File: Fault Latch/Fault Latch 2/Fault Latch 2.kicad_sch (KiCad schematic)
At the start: 47 parts, among them J1 Inputs, K1 Fujitsu_FTR-LYAA005x, K2 Fujitsu_FTR-LYAA005x, K3 Fujitsu_FTR-LYAA005x, Q1 PMOS, Q2 PMOS, Q3 PMOS, Q4 NMOS, Q5 PMOS, Q6 PMOS, Q7 PMOS, Q8 NMOS, Q9 PMOS, SW1 SW_Push_Dual_x2, SW2 SW_Push_Dual_x2, SW4 SW_Push_Dual_x2, U1 74LS279, U10 74LS279, U11 4N35, U2 74AHC1G04, U3 74AHC1G04, U5 74LS279, U7 4N35, U8 4N35, U9 74AHC1G04

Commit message: Edits to Fault Latch and TSSI
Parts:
- removed D3: LED, symbol Device:LED
- removed Q1, Q2, Q3, Q6: PMOS, symbol Simulation_SPICE:PMOS
- removed R1: 2.2k, symbol Device:R_US
- removed R2, R4: R_US, symbol Device:R_US
- removed SW2, SW4: SW_Push_Dual_x2, symbol Switch:SW_Push_Dual_x2
- removed U1, U10, U5: 74LS279, symbol 74xx:74LS279
- removed U11, U7, U8: 4N35, Package_DIP:DIP-6_W7.62mm, symbol Isolator:4N35
- removed U3: 74AHC1G04, symbol 74xGxx:74AHC1G04
- added C101: 100n, symbol Device:C
- added C102: ?, symbol Device:C
- added D101: LED, symbol Device:LED
- added Q101, Q104, Q108: NMOS, symbol Simulation_SPICE:NMOS
- added R101, R102, R107, R108: 10k, symbol Device:R_US
- added R103: 500R, symbol Device:R_US
- added R106: 2.2k, symbol Device:R_US
- added R109: ?, symbol Device:R_US
- added R114: R_US, symbol Device:R_US
- added U103: 74AHC1G00, symbol 74xGxx:74AHC1G00
- added U104: 74LS279, symbol 74xx:74LS279
- added U105: SFH617A-1, Package_DIP:DIP-4_W7.62mm, symbol Isolator:SFH617A-1
- renumbered D1 to D102, D4 to D103, D5 to D104, D6 to D105, D2 to D106, J1 to J101, J4 to J102, J3 to J103, J2 to J104, K3 to K101, K2 to K102, K1 to K103, Q8 to Q102, Q4 to Q103, Q7 to Q105, Q9 to Q106, Q5 to Q107, R3 to R104, R8 to R105, R6 to R110, R9 to R111, R7 to R112, R5 to R113, R10 to R115, R13 to R116, R12 to R117, R11 to R118, SW1 to SW101, U2 to U101, U9 to U102
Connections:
- net +5V: now also R103.1, R107.1, R108.2, R114.2, U103.5 (VCC), U104.16 (VCC); no longer D106.1 (K), K103.A1
- net BSPD: now also R102.1
- net GND: now also SW101.1 (C), C102.2, Q101.3 (S), Q104.3 (S), Q108.3 (S), R102.2, R106.2, U103.3 (GND), U104.8 (GND), U105.3; no longer R115.1
- net IMD: now also R106.1
- net Shutdown Circuit: no longer J104.1 (Pin_1), K103.13
- net at D106.2 (A), K103.A2: now also Q108.1 (D)
- net +12V: now reaches R115.2
- net +12V: now also D106.1 (K), K103.A1, R101.1
- net at SW101.2 (D): now also R108.1, R109.2
- net at D104.2 (A), K102.A2: no longer Q107.1 (D)
- net BMS renamed NBMS
- net NBMS: now also R101.2
- new net: C101.2, D101.1 (K), Q101.1 (D), Q104.2 (G)
- new net: J104.1 (Pin_1), K103.13
- new net: Q108.2 (G), R115.1, U105.4
- new net: C101.1, D101.2 (A), R103.2
- new net: U103.4, U104.2 (~{S}), U104.3 (~{S})
- new net: R114.1, U105.1
- new net: U104.4 (Q), U105.2
- new net NBMS_HV: Q101.2 (G)
- new net NBMS_LV: Q104.1 (D), R107.2, U103.1, U104.1 (~{R})
- new net NRESET: C102.1, R109.1, U103.2
- no-connect marks 4 -> 3
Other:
- note added: "16mA MAX"
- note added: "I think FSAE says relays need to be normally activated?"
- note added: "Open collector pull ups/downs should be provided on this board only!"
- note added: "When nR pulsed low (fault), Q pulled low Undefined when both inputs low"
- moved on the sheet: D102, D103, D104, D105, D106, J102, J103, J104, K101, K102, K103, Q102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

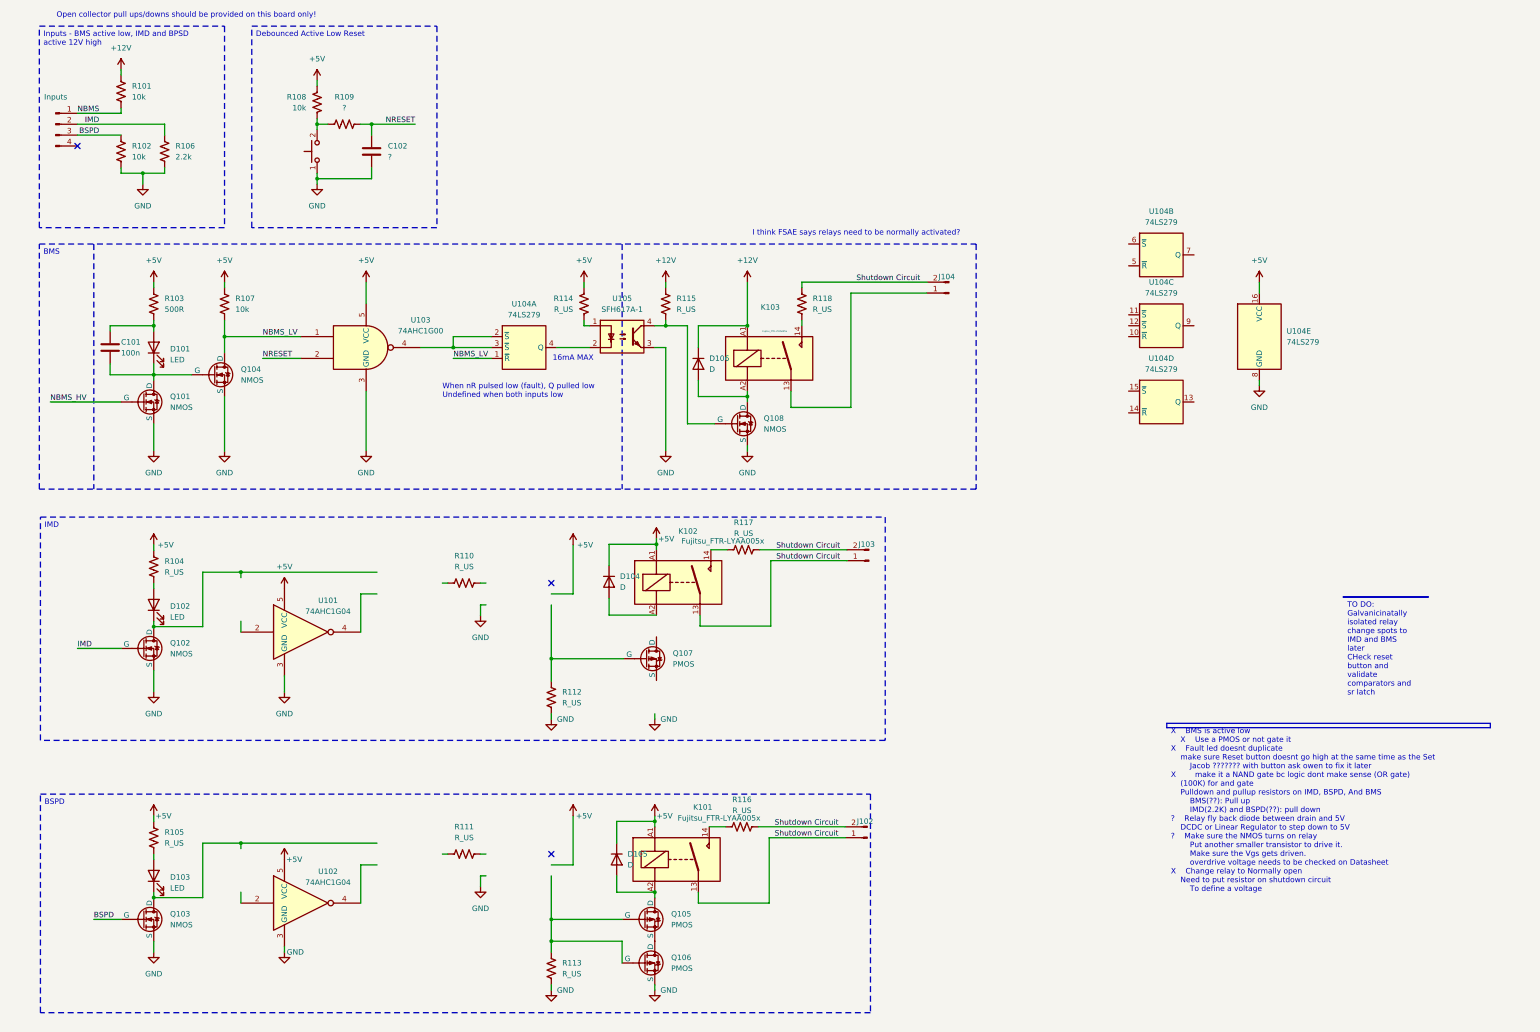
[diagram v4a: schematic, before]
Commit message: Fixed the logic for IMD and BSPD
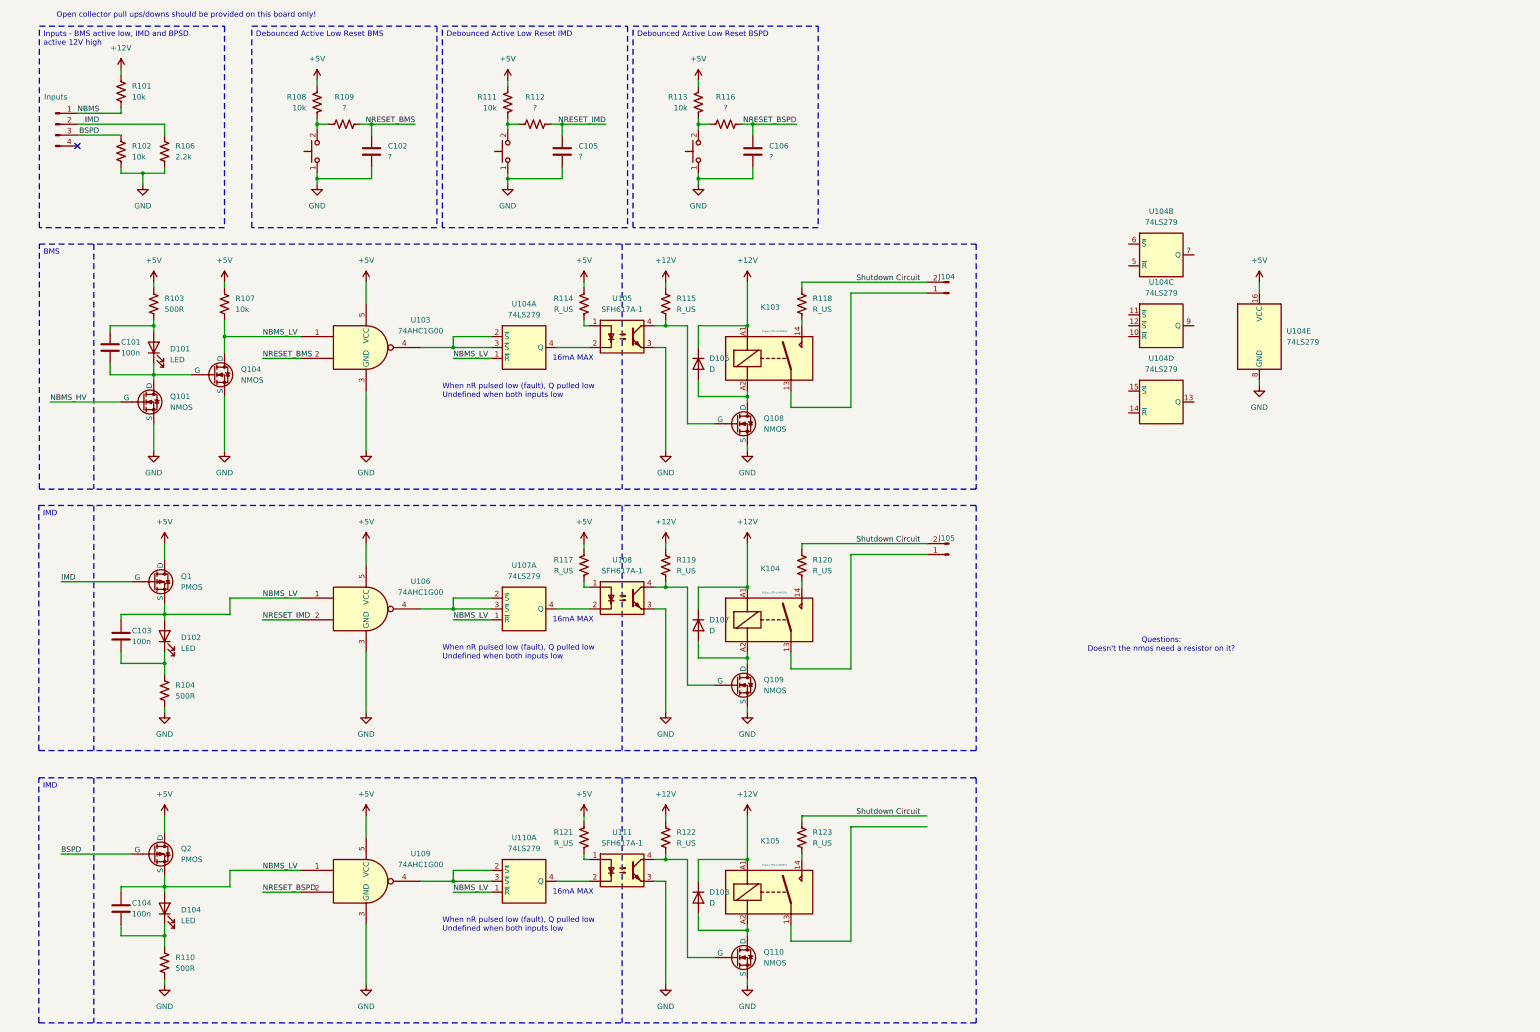
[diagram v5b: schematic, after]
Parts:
- removed D103: LED, symbol Device:LED
- removed D104, D105: D, symbol Device:D
- removed J102, J103: ~, symbol Connector:Conn_01x02_Pin
- removed K101, K102: Fujitsu_FTR-LYAA005x, Relay_THT:Relay_SPST-NO_Fujitsu_FTR-LYAA005x_FormA_Vertical, symbol Relay:Fujitsu_FTR-LYAA005x
- removed Q102, Q103: NMOS, symbol Simulation_SPICE:NMOS
- removed Q105, Q106, Q107: PMOS, symbol Simulation_SPICE:PMOS
- removed R105: R_US, symbol Device:R_US
- removed U101, U102: 74AHC1G04, symbol 74xGxx:74AHC1G04
- added C103, C104: 100n, symbol Device:C
- added C105, C106: ?, symbol Device:C
- added D104: LED, symbol Device:LED
- added D107, D108: D, symbol Device:D
- added J105: ~, symbol Connector:Conn_01x02_Pin
- added K104, K105: Fujitsu_FTR-LYAA005x, Relay_THT:Relay_SPST-NO_Fujitsu_FTR-LYAA005x_FormA_Vertical, symbol Relay:Fujitsu_FTR-LYAA005x
- added Q1, Q2: PMOS, symbol Simulation_SPICE:PMOS
- added Q109, Q110: NMOS, symbol Simulation_SPICE:NMOS
- added R119, R120, R121, R122, R123: R_US, symbol Device:R_US
- added SW102, SW103: SW_Push_Dual_x2, symbol Switch:SW_Push_Dual_x2
- added U106, U109: 74AHC1G00, symbol 74xGxx:74AHC1G00
- added U107, U110: 74LS279, symbol 74xx:74LS279
- added U108, U111: SFH617A-1, Package_DIP:DIP-4_W7.62mm, symbol Isolator:SFH617A-1
- R104, R110: value R_US -> 500R
- R111, R113: value R_US -> 10k
- R112, R116: value R_US -> ?
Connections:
- net +12V: now also D107.1 (K), D108.1 (K), K104.A1, K105.A1, R119.2, R122.2
- net +5V: now also R111.2, R113.2, R117.2, Q1.1 (D), Q2.1 (D), R121.2, U106.5 (VCC), U109.5 (VCC); no longer R104.1
- net BSPD: now also Q2.2 (G)
- net GND: now also R104.2, R110.2, C105.2, C106.2, Q109.3 (S), Q110.3 (S), SW102.1 (C), SW103.1 (C), U106.3 (GND), U108.3, U109.3 (GND), U111.3; no longer R112.1, R113.1
- net IMD: now also Q1.2 (G)
- net NBMS_LV: now also D102.2 (A), C103.1, C104.1, D104.2 (A), Q1.3 (S), Q2.3 (S), U106.1, U107.1 (~{R}), U109.1, U110.1 (~{R})
- net Shutdown Circuit: now also J105.2 (Pin_2), R120.2, R123.2; no longer R116.2, R117.2
- net at D102.1 (K): now also R104.1, C103.2
- net at R111.1: now also R112.2, SW102.2 (D)
- net at R117.1: now also U108.1
- net NRESET_BSPD: now reaches R116.1
- net NRESET_BSPD: now also C106.1, U109.2
- net at R110.1: now also C104.2, D104.1 (K)
- net NRESET renamed NRESET_BMS
- new net: K105.14, R123.1
- new net: R121.1, U111.1
- new net: D108.2 (A), K105.A2, Q110.1 (D)
- new net: R113.1, R116.2, SW103.2 (D)
- new net: U109.4, U110.2 (~{S}), U110.3 (~{S})
- new net: U110.4 (Q), U111.2
- new net: D107.2 (A), K104.A2, Q109.1 (D)
- new net: Q109.2 (G), R119.1, U108.4
- new net: U106.4, U107.2 (~{S}), U107.3 (~{S})
- new net: Q110.2 (G), R122.1, U111.4
- new net: J105.1 (Pin_1), K104.13
- new net: U107.4 (Q), U108.2
- new net: K104.14, R120.1
- new net NRESET_IMD: C105.1, R112.1, U106.2
- no-connect marks 3 -> 1
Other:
- note added: "Questions: Doesn't the nmos need a resistor on it?"
- note removed: "I think FSAE says relays need to be normally activated?"

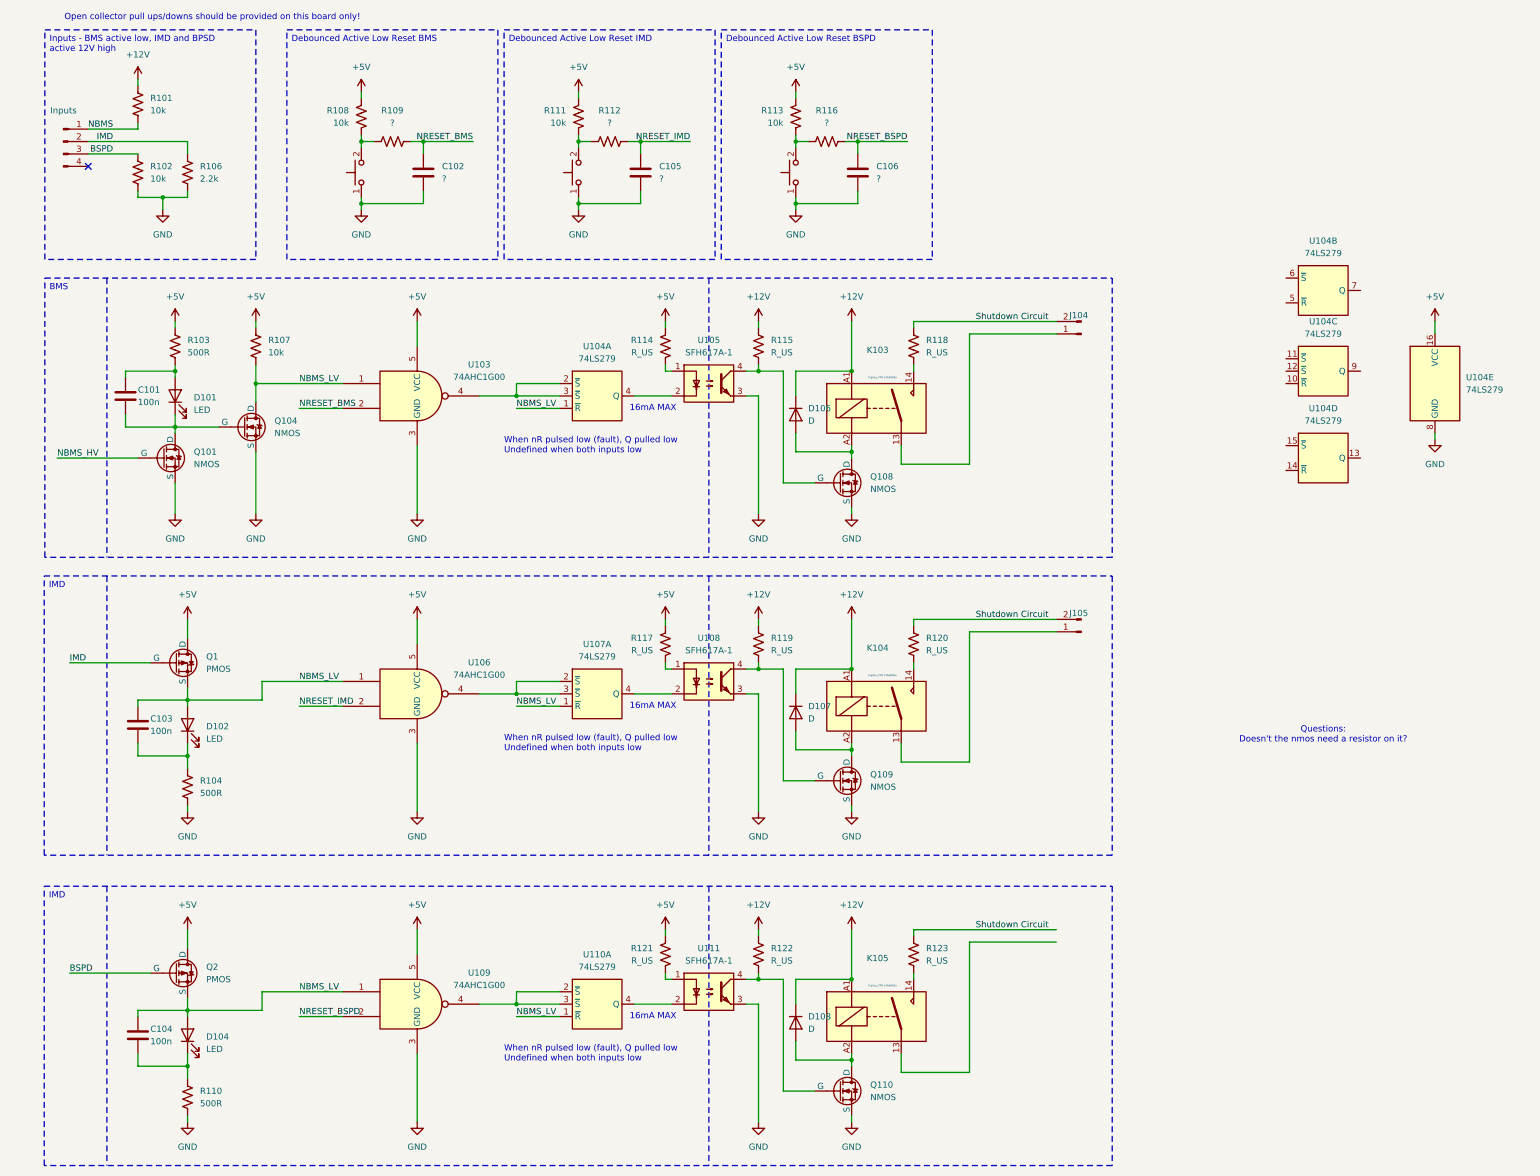
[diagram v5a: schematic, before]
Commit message: Added some footprints but also realized stuff about rules we need to change fault latch for
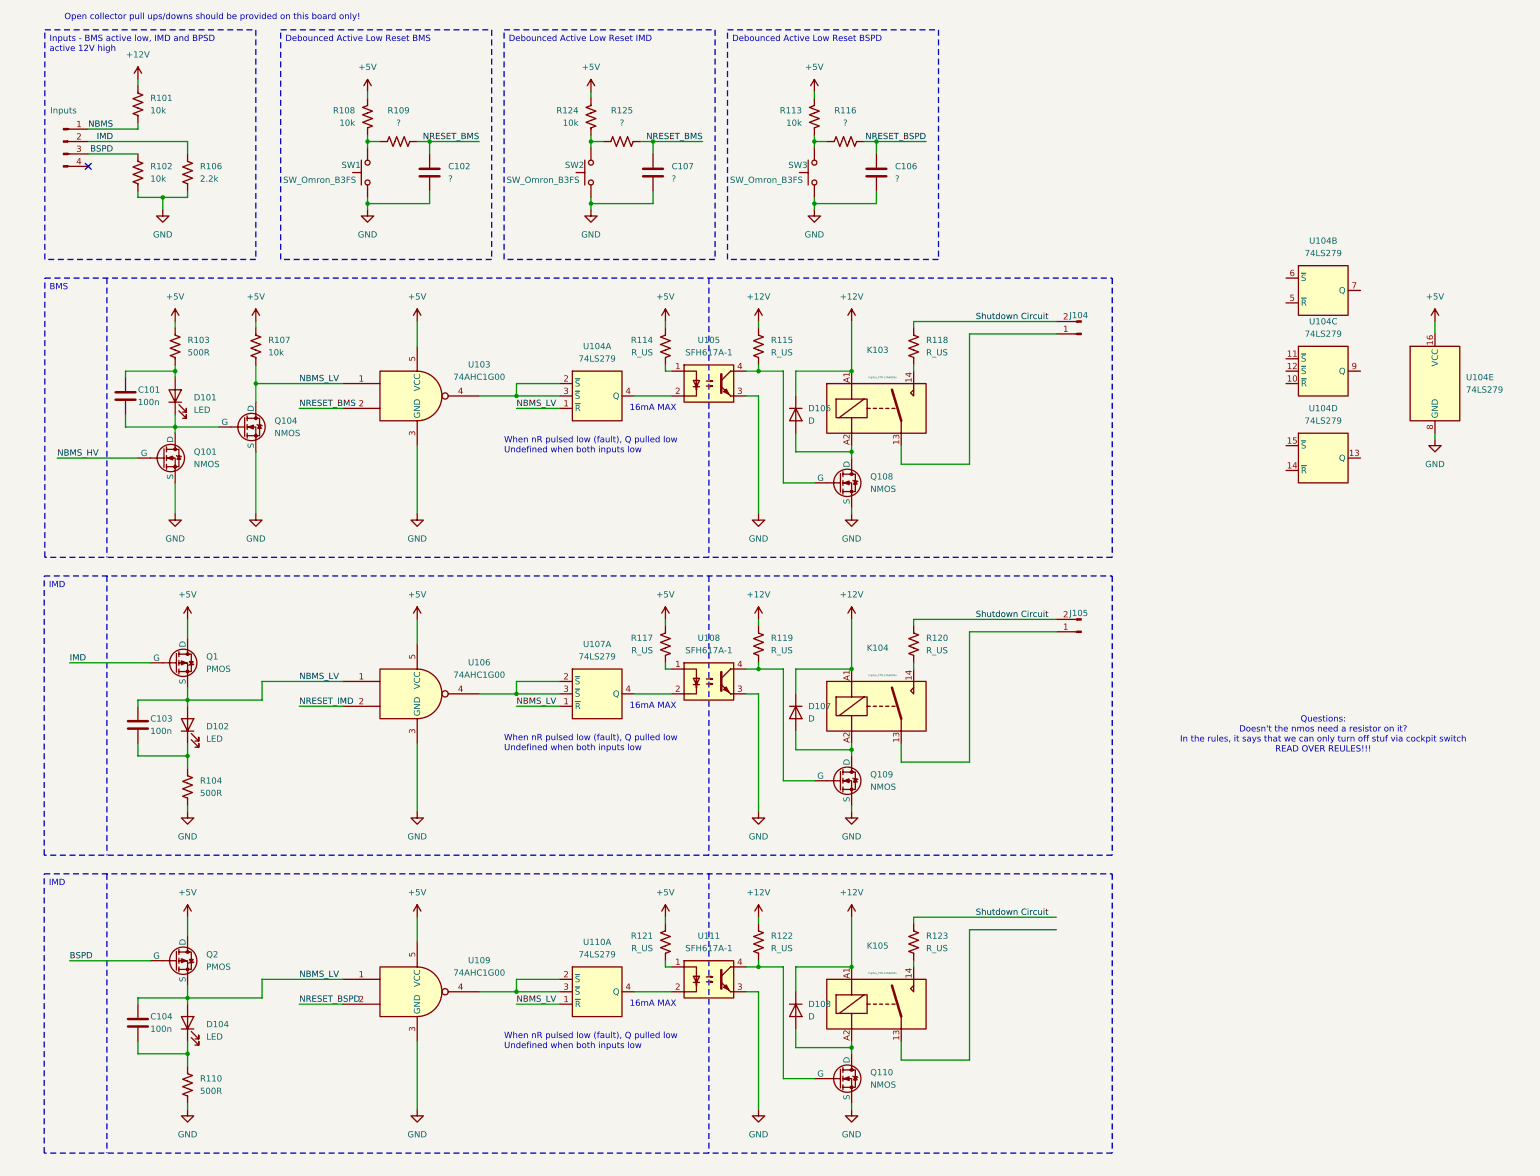
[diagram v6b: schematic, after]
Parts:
- removed C105: ?, symbol Device:C
- removed R111: 10k, symbol Device:R_US
- removed R112: ?, symbol Device:R_US
- removed SW101, SW102, SW103: SW_Push_Dual_x2, symbol Switch:SW_Push_Dual_x2
- added C107: ?, symbol Device:C
- added R124: 10k, symbol Device:R_US
- added R125: ?, symbol Device:R_US
- added SW1, SW2, SW3: SW_Omron_B3FS, Button_Switch_SMD:SW_SPST_Omron_B3FS-100xP, symbol Switch:SW_Omron_B3FS
- D101, D102, D104: footprint (none) -> LED_SMD:LED_0201_0603Metric; JLC# (none) -> IN-S21AT2G
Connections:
- net +5V: now also R124.2
- net GND: now also C107.2, SW1.1, SW2.1, SW3.1
- net NRESET_BMS: now also C107.1, R125.1
- net at R108.1, R109.2: now also SW1.2
- net at R113.1, R116.2: now also SW3.2
- new net: R124.1, R125.2, SW2.2
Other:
- note added: "Questions: Doesn't the nmos need a resistor on it? In the rules, it says that we can only turn off stuf via cockpit switch READ OVER REULES!!!"
- note removed: "Questions: Doesn't the nmos need a resistor on it?"
- moved on the sheet: C102, C104, C106, D104, D108, K105, Q110, Q2, R108, R109, R110, R113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

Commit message: TSSI and FL fixes
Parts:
- removed C101, C103, C104: 100n, symbol Device:C
- removed R118, R120, R123: R_US, symbol Device:R_US
- removed U107, U110: 74LS279, symbol 74xx:74LS279
- U104: footprint (none) -> Package_SO:SOIC-16_3.9x9.9mm_P1.27mm
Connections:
- net NBMS_LV: no longer D102.2 (A), D104.2 (A), Q1.3 (S), Q2.3 (S), U106.1, U109.1
- net NRESET_BMS: no longer C107.1, R125.1
- net NRESET_BSPD: no longer C106.1, R116.1
- net Shutdown Circuit: now also K103.14, K104.14, K105.14
- net at U104.11 (~{S}): now also U104.12 (~{S}), U109.4
- net at U104.9 (Q): now also U111.2
- net at U106.4: now also U104.6 (~{S})
- net at U104.7 (Q): now also U108.2
- new net: D104.2 (A), Q2.3 (S), U109.1
- new net: D102.2 (A), Q1.3 (S), U106.1
- new net: C107.1, R125.1
- new net: C106.1, R116.1
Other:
- note added: "3/12/25 NOTES - Put decoupling caps on 74LS279 - Place resistors on coil according to datasheet - Pulse generator"
- moved on the sheet: U104B, U104C, U104D, U104E
